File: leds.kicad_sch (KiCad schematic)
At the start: 42 parts

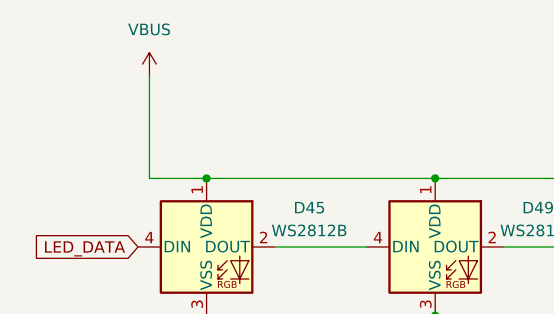
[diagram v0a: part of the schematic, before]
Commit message: Atreus Low Profile PCB Version 1.0.0
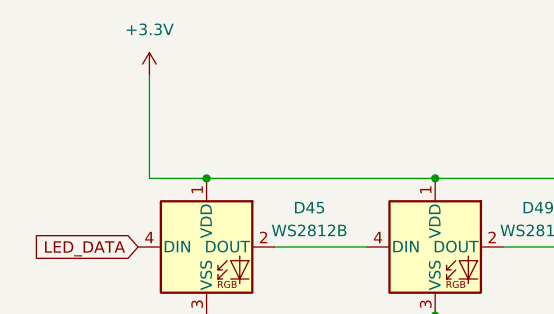
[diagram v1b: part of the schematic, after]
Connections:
- net VBUS renamed +3V3
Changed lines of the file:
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@@
     (pin "4")
-  )
-  (symbol (lib_id "power:VBUS") (at 21.59 22.86 0) (unit 1)
-    (in_bom yes) (on_board yes) (fields_autoplaced)
-    (property "Reference" "#PWR032" (id 0) (at 21.59 26.67 0)
-      (effects (font (size 1.27 1.27)) hide)
-    )
-    (property "Value" "VBUS" (id 1) (at 21.59 17.78 0))
-    (property "Footprint" "" (id 2) (at 21.59 22.86 0)
-      (effects (font (size 1.27 1.27)) hide)
-    )
-    (property "Datasheet" "" (id 3) (at 21.59 22.86 0)
-      (effects (font (size 1.27 1.27)) hide)
-    )
-    (pin "1")
   )
   (symbol (lib_id "LED:WS2812B") (at 177.8 109.22 0) (unit 1)
@@
     (pin "4")
   )
+  (symbol (lib_id "power:+3.3V") (at 21.59 22.86 0) (unit 1)
+    (in_bom yes) (on_board yes) (fields_autoplaced)
+    (property "Reference" "#PWR06" (id 0) (at 21.59 26.67 0)
+      (effects (font (size 1.27 1.27)) hide)
+    )
+    (property "Value" "+3.3V" (id 1) (at 21.59 17.78 0))
+    (property "Footprint" "" (id 2) (at 21.59 22.86 0)
+      (effects (font (size 1.27 1.27)) hide)
+    )
+    (property "Datasheet" "" (id 3) (at 21.59 22.86 0)
+      (effects (font (size 1.27 1.27)) hide)
+    )
+    (pin "1")
+  )
   (symbol (lib_id "LED:WS2812B") (at 27.94 41.91 0) (unit 1)
